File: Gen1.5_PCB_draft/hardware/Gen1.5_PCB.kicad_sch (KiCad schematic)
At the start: 0 parts

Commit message: added components
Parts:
- added J1: ESP32_P4, symbol Gen1.5_PCB:ESP32_P4
- added J2: IMU, symbol Connector_Generic:Conn_01x04
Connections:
- new net LC1: J1.20 (GPIO20)
- new net LC2: J1.21 (GPIO21)
- new net LC3: J1.22 (GPIO22)
- new net LC4: J1.23 (GPIO23)
- new net LS1: J1.16 (GPIO16)
- new net LS2: J1.17 (GPIO17)
- new net LS3: J1.18 (GPIO18)
- new net LS4: J1.19 (GPIO19)
- new net RX1: J1.3 (GPIO3)
- new net RX2: J1.5 (GPIO5)
- new net RX3: J1.14 (GPIO14)
- new net SCL: J1.8 (SCL/GPIO8), J2.4 (Pin_4)
- new net SDA: J1.7 (SDA/GPIO7), J2.3 (Pin_3)
- new net TX1: J1.2 (GPIO2)
- new net TX2: J1.4 (GPIO4)
- new net TX3: J1.6 (GPIO6)

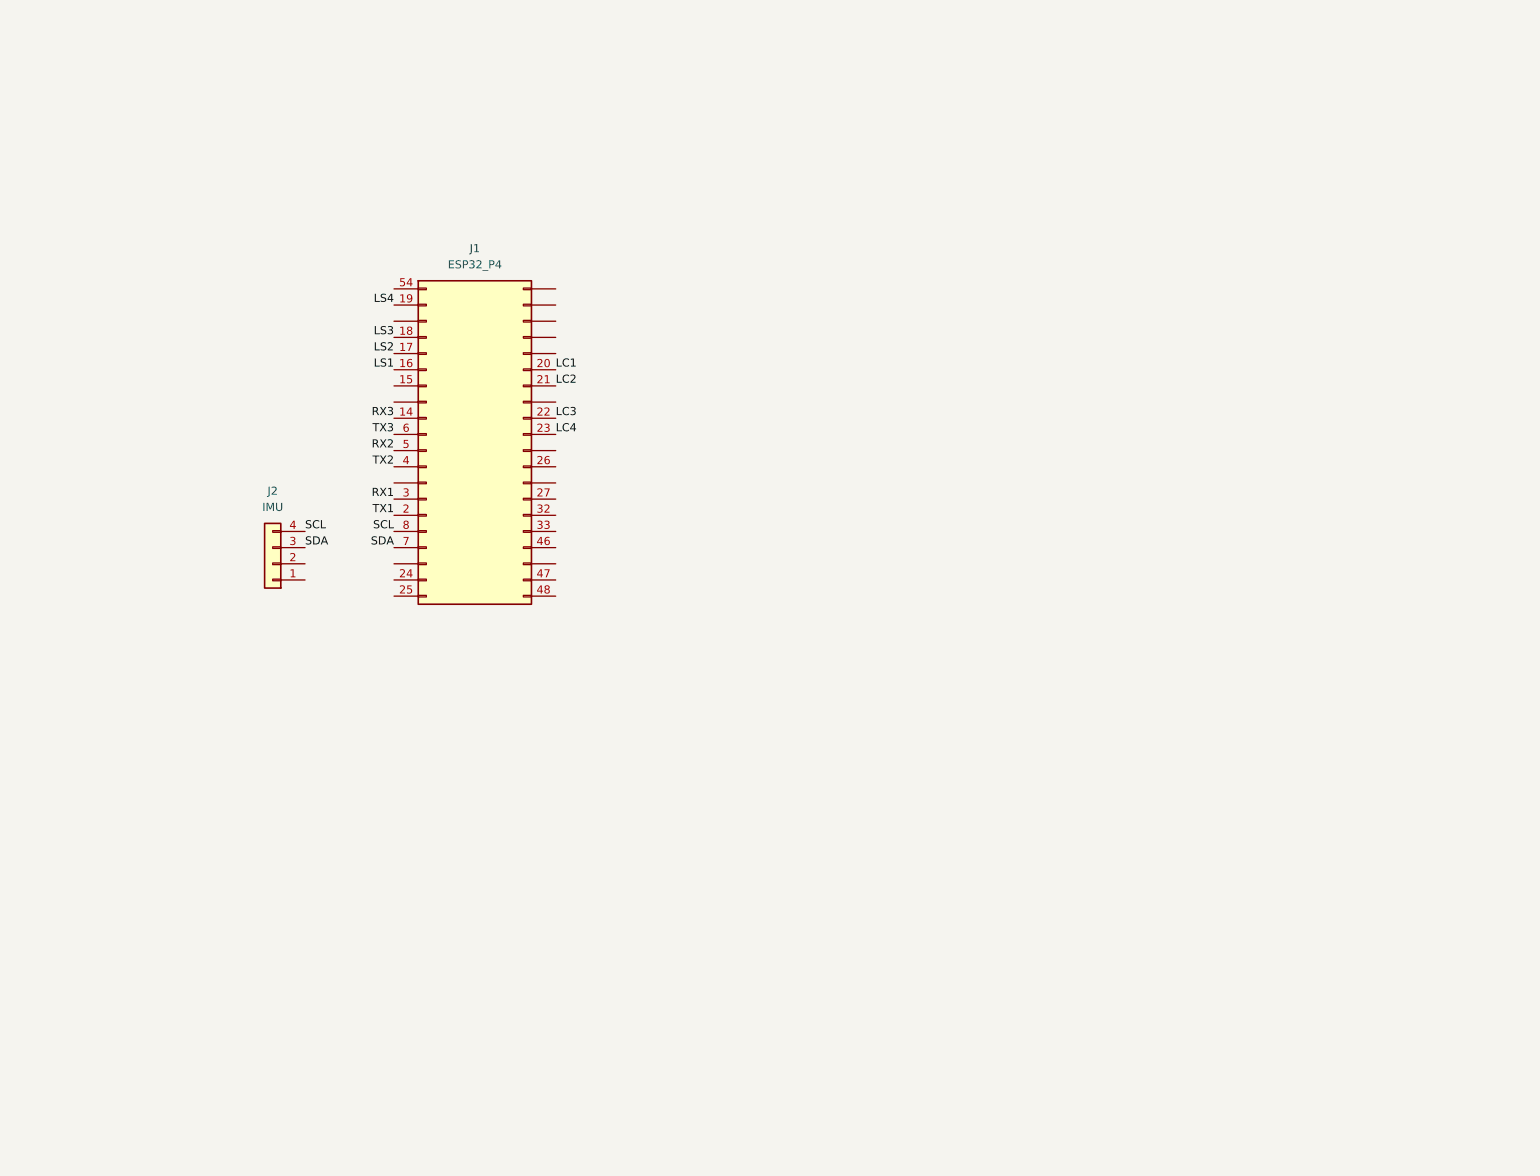
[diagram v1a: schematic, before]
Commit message: components added to sch
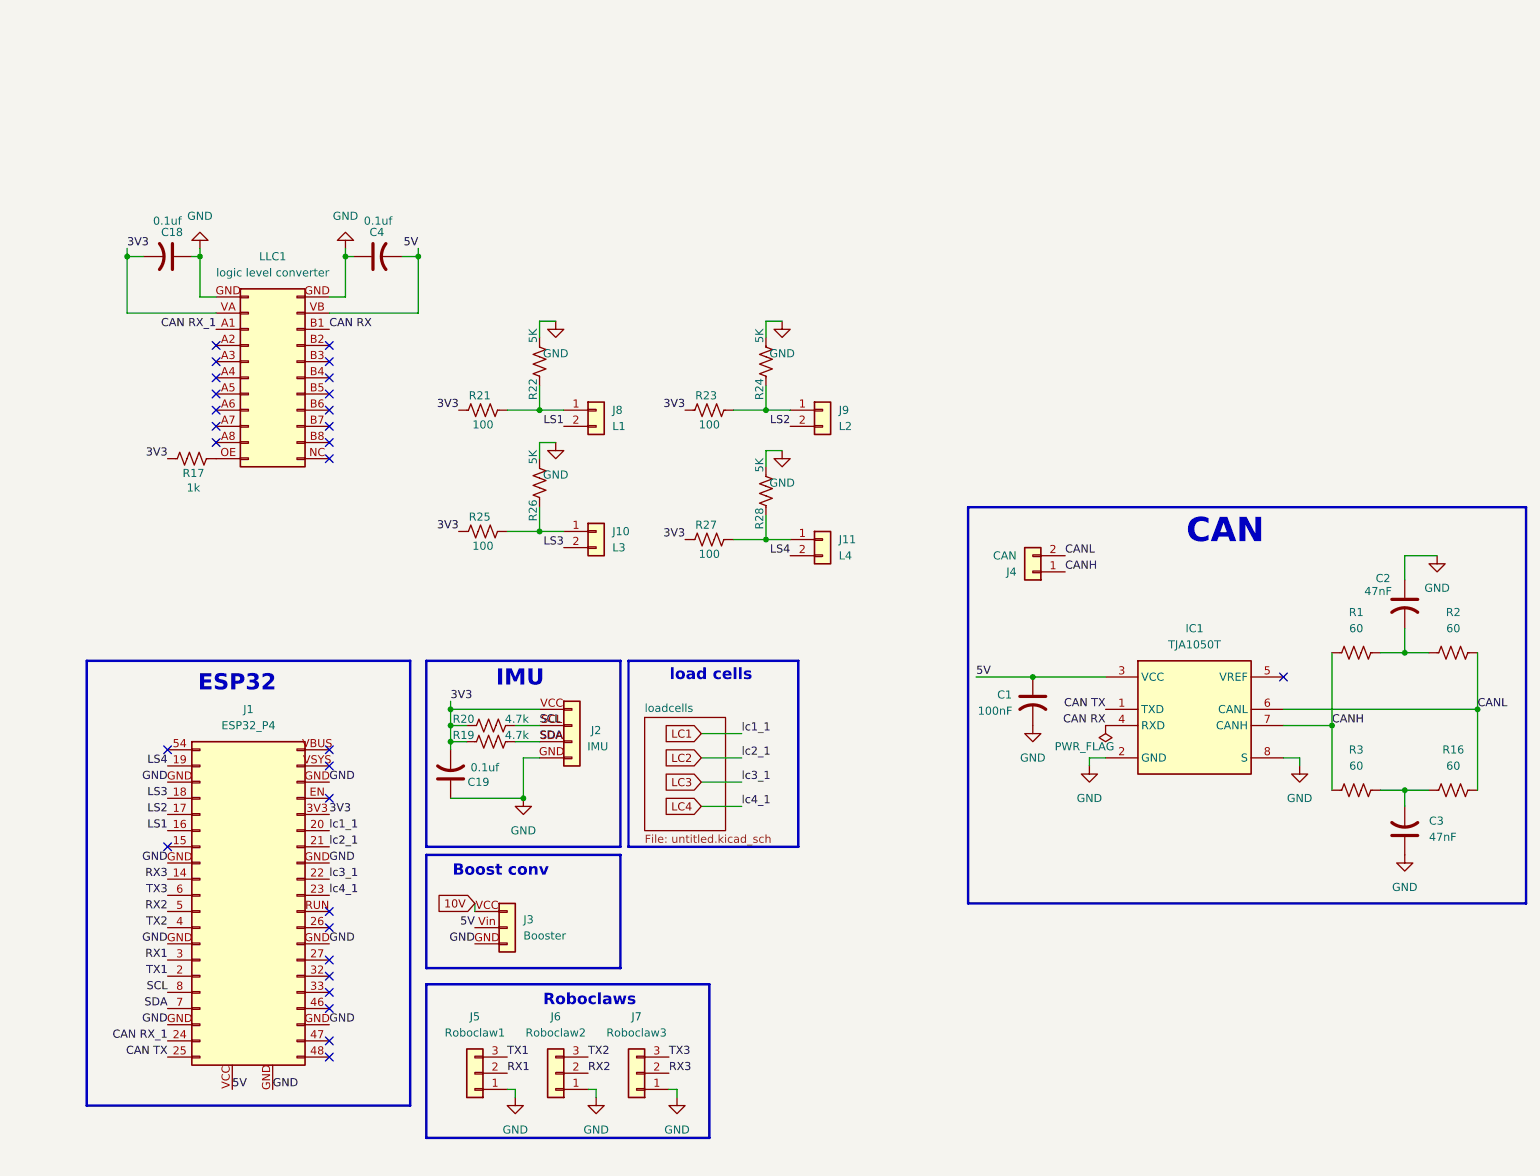
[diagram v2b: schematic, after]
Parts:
- added C1: 100nF, symbol Device:C_US
- added C18, C19, C4: 0.1uf, symbol Device:C_US
- added C2, C3: 47nF, symbol Device:C_US
- added IC1: TJA1050T, Gen1.5_PCB:TJA1050T, symbol Gen1.5_PCB:TJA1050T
- added J10: L3, symbol Connector_Generic:Conn_01x02
- added J11: L4, symbol Connector_Generic:Conn_01x02
- added J3: Booster, symbol Connector_Generic:Conn_01x03
- added J4: CAN, symbol Connector_Generic:Conn_01x02
- added J5: Roboclaw1, symbol Connector_Generic:Conn_01x03
- added J6: Roboclaw2, symbol Connector_Generic:Conn_01x03
- added J7: Roboclaw3, symbol Connector_Generic:Conn_01x03
- added J8: L1, symbol Connector_Generic:Conn_01x02
- added J9: L2, symbol Connector_Generic:Conn_01x02
- added LLC1: logic level converter, symbol Gen1.5_PCB:logic_level_converter
- added R1, R16, R2, R3: 60, symbol Device:R_US
- added R17: 1k, symbol Device:R_US
- added R19, R20: 4.7k, symbol Device:R_US
- added R21, R23, R25, R27: 100, symbol Device:R_US
- added R22, R24, R26, R28: 5K, symbol Device:R_US
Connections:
- net LS1: now also J8.2 (Pin_2)
- net LS2: now also J9.2 (Pin_2)
- net LS3: now also J10.2 (Pin_2)
- net LS4: now also J11.2 (Pin_2)
- net RX1: now also J5.2 (Pin_2)
- net RX2: now also J6.2 (Pin_2)
- net RX3: now also J7.2 (Pin_2)
- net SCL: now also J2.SCL (Pin_2), R20.2; no longer J2.4 (Pin_4)
- net SDA: now also J2.SDA (Pin_3), R19.2; no longer J2.3 (Pin_3)
- net TX1: now also J5.3 (Pin_3)
- net TX2: now also J6.3 (Pin_3)
- net TX3: now also J7.3 (Pin_3)
- net CAN RX_1: now reaches J1.24 (DM/GPIO24)
- net CAN RX_1: now also LLC1.A1 (Pin_3)
- net CAN TX: now reaches J1.25 (DP/GPIO25)
- net CAN TX: now also IC1.1 (TXD)
- new net: LLC1.OE (Pin_11), R17.2
- new net: J11.1 (Pin_1), R27.2, R28.1
- new net: J10.1 (Pin_1), R25.2, R26.1
- new net: C2.2, R1.2, R2.1
- new net: J9.1 (Pin_1), R23.2, R24.1
- new net: C3.2, R16.1, R3.2
- new net: J8.1 (Pin_1), R21.2, R22.1
- new net 10V: J3.VCC
- new net 3V3: C18.2, C19.2, J1.3V3, J2.VCC (Pin_1), LLC1.VA (Pin_2), R17.1, R19.1, R20.1, R21.1, R23.1, R25.1, R27.1
- new net 5V: C1.1, C4.2, IC1.3 (VCC), J1.VCC, J3.Vin, LLC1.VB (Pin_21)
- new net CAN RX: IC1.4 (RXD), LLC1.B1 (Pin_20)
- new net CANH: IC1.7 (CANH), J4.1 (Pin_1), R1.1, R3.1
- new net CANL: IC1.6 (CANL), J4.2 (Pin_2), R16.2, R2.2
- new net GND: C1.2, C18.1, C19.1, C2.1, C3.1, C4.1, IC1.2 (GND), IC1.8 (S), J1.GND, J2.GND (Pin_4), J3.GND, J5.1 (Pin_1), J6.1 (Pin_1), J7.1 (Pin_1), LLC1.GND (Pin_22), R22.2, R24.2, R26.2, R28.2
- no-connect marks 0 -> 29
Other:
- added sheet loadcells (untitled.kicad_sch)
- note added: "Boost conv"
- note added: "CAN"
- note added: "ESP32"
- note added: "IMU"
- note added: "Roboclaws"
- note added: "load cells"

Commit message: moved imu header to spi
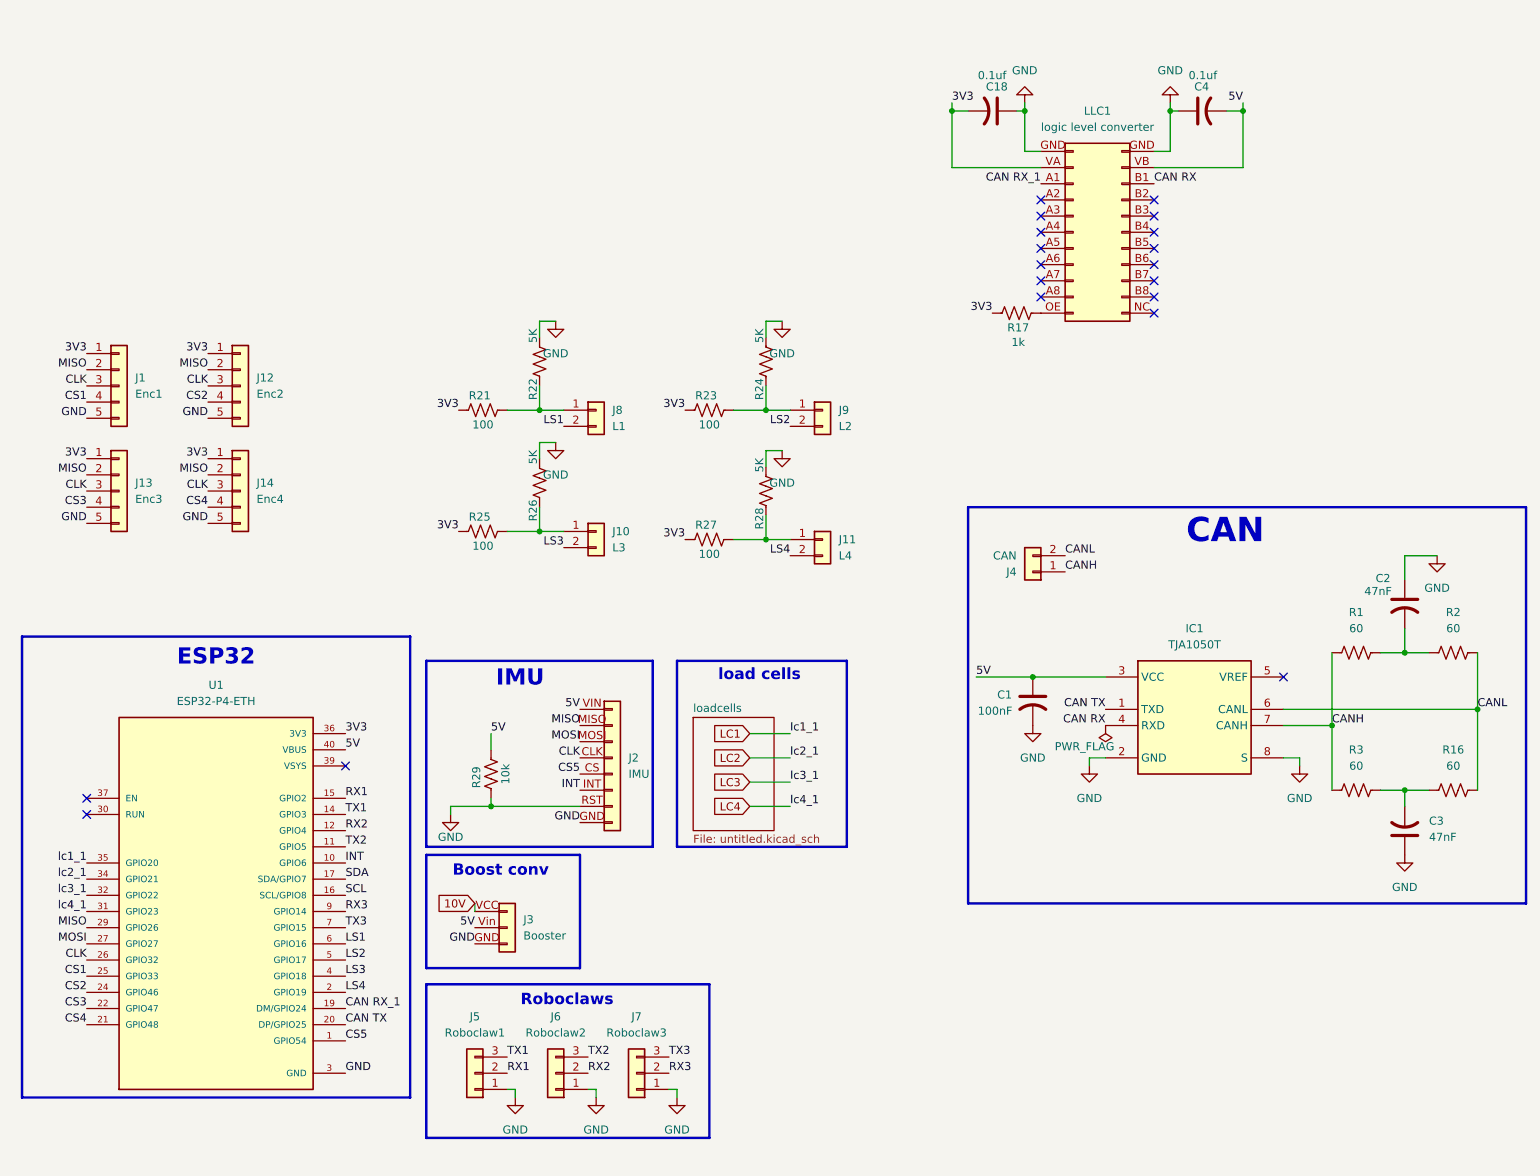
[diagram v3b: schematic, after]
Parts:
- removed C19: 0.1uf, symbol Device:C_US
- removed J1: ESP32_P4, symbol Gen1.5_PCB:ESP32_P4
- removed J2: IMU, symbol Connector_Generic:Conn_01x04
- removed R19, R20: 4.7k, symbol Device:R_US
- added J1: Enc1, symbol Connector_Generic:Conn_01x05
- added J12: Enc2, symbol Connector_Generic:Conn_01x05
- added J13: Enc3, symbol Connector_Generic:Conn_01x05
- added J14: Enc4, symbol Connector_Generic:Conn_01x05
- added J2: IMU, symbol Connector_Generic:Conn_01x08
- added R29: 10k, symbol Device:R_US
- added U1: ESP32-P4-ETH, ESP32-P4-ETH:MODULE_ESP32-P4-ETH, symbol Gen1.5_PCB:ESP32-P4-ETH
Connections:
- net 3V3: now also J1.1 (Pin_1), J12.1 (Pin_1), J13.1 (Pin_1), J14.1 (Pin_1), U1.36 (3V3)
- net 5V: now also J2.VIN (Pin_1), R29.2, U1.40 (VBUS)
- net CAN RX_1: now also U1.19 (DM/GPIO24)
- net CAN TX: now also U1.20 (DP/GPIO25)
- net GND: now also J1.5 (Pin_5), J12.5 (Pin_5), J13.5 (Pin_5), J14.5 (Pin_5), J2.GND (Pin_8), J2.RST (Pin_7), R29.1, U1.13 (GND), U1.18 (GND), U1.23 (GND), U1.28 (GND), U1.3 (GND), U1.33 (GND), U1.38 (GND), U1.8 (GND)
- net LC1: now also U1.35 (GPIO20)
- net LC2: now also U1.34 (GPIO21)
- net LC3: now also U1.32 (GPIO22)
- net LC4: now also U1.31 (GPIO23)
- net LS1: now also U1.6 (GPIO16)
- net LS2: now also U1.5 (GPIO17)
- net LS3: now also U1.4 (GPIO18)
- net LS4: now also U1.2 (GPIO19)
- net RX1: now also U1.15 (GPIO2)
- net RX2: now also U1.12 (GPIO4)
- net RX3: now also U1.9 (GPIO14)
- net SCL: now also U1.16 (SCL/GPIO8)
- net SDA: now also U1.17 (SDA/GPIO7)
- net TX1: now also U1.14 (GPIO3)
- net TX2: now also U1.11 (GPIO5)
- net TX3: now also U1.7 (GPIO15)
- new net CLK: J1.3 (Pin_3), J12.3 (Pin_3), J13.3 (Pin_3), J14.3 (Pin_3), J2.CLK (Pin_4), U1.26 (GPIO32)
- new net CS1: J1.4 (Pin_4), U1.25 (GPIO33)
- new net CS2: J12.4 (Pin_4), U1.24 (GPIO46)
- new net CS3: J13.4 (Pin_4), U1.22 (GPIO47)
- new net CS4: J14.4 (Pin_4), U1.21 (GPIO48)
- new net CS5: J2.CS (Pin_5), U1.1 (GPIO54)
- new net INT: J2.INT (Pin_6), U1.10 (GPIO6)
- new net MISO: J1.2 (Pin_2), J12.2 (Pin_2), J13.2 (Pin_2), J14.2 (Pin_2), J2.MISO (Pin_2), U1.29 (GPIO26)
- new net MOSI: J2.MOSI (Pin_3), U1.27 (GPIO27)
- no-connect marks 29 -> 19
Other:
- moved on the sheet: C18, C4, LLC1, R17

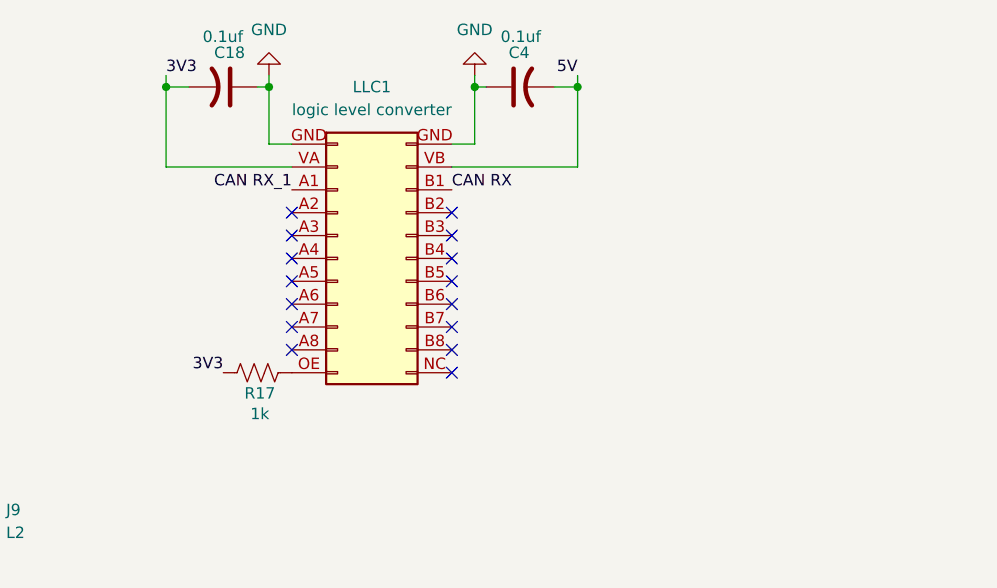
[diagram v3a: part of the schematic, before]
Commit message: switched level shifter to single i/o level shifter
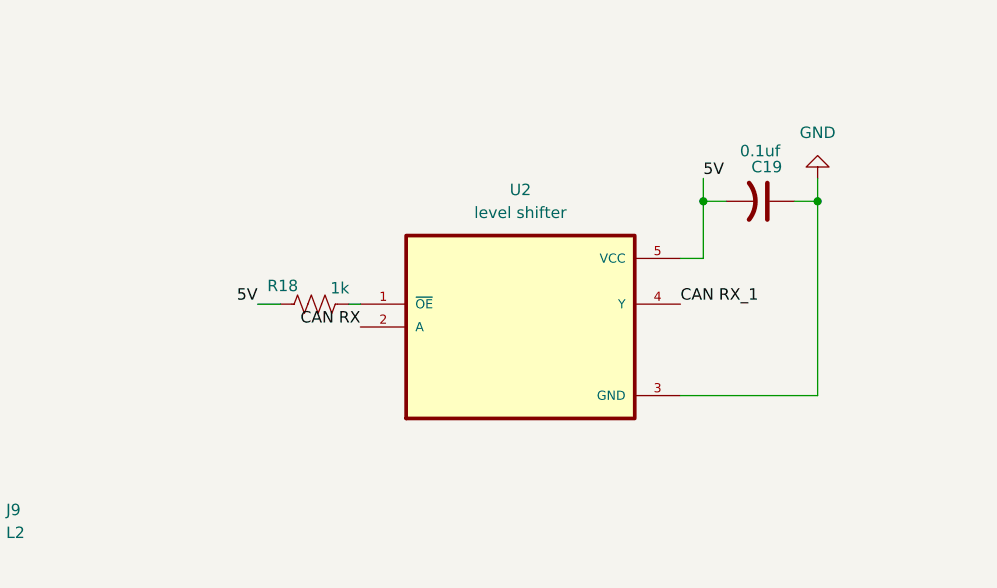
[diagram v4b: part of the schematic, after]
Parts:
- removed C18, C4: 0.1uf, symbol Device:C_US
- removed LLC1: logic level converter, symbol Gen1.5_PCB:logic_level_converter
- removed R17: 1k, symbol Device:R_US
- added C19: 0.1uf, symbol Device:C_US
- added R18: 1k, symbol Device:R_US
- added U2: level shifter, SN74LVC1G125DBVR:SOT95P280X145-5N, symbol Gen1.5_PCB:SN74LVC1G125DBVR
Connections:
- net 5V: now also C19.2, R18.1, U2.5 (VCC)
- net CAN RX: now also U2.2 (A)
- net CAN RX_1: now also U2.4 (Y)
- net GND: now also C19.1, U2.3 (GND)
- new net: R18.2, U2.1 (~{OE})
- no-connect marks 19 -> 4
